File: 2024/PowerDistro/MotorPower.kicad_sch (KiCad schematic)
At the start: 8 parts, among them J1 10159560-A00221RLF, J2 10159560-A00221RLF, J3 10159560-A00221RLF, J4 10159560-A00221RLF, J5 10159560-A00221RLF, J6 10159560-A00221RLF, J7 10159560-A00221RLF, J8 10159560-A00221RLF

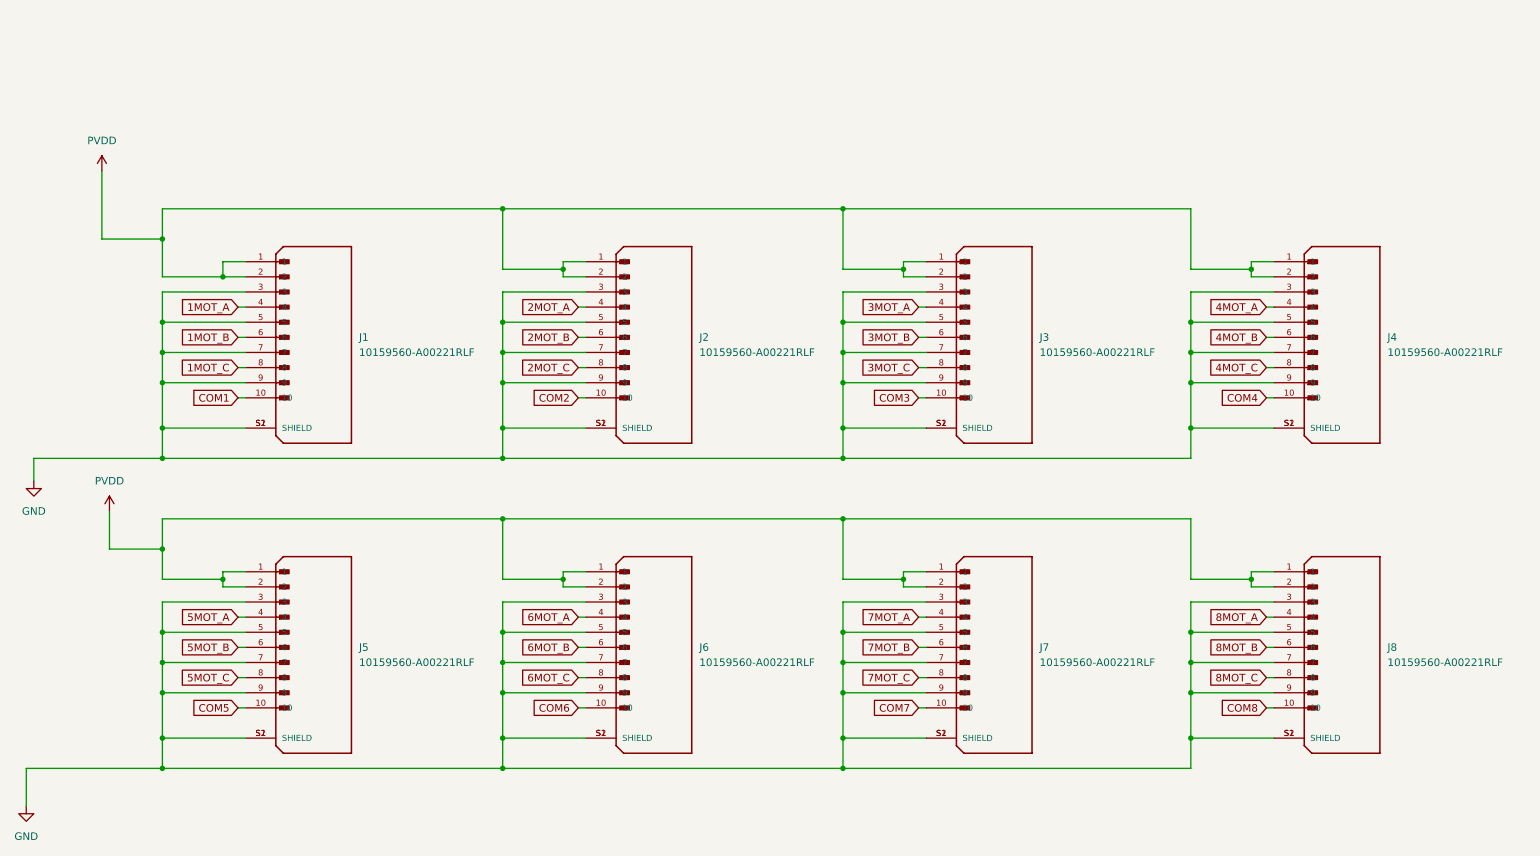
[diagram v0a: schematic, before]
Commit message: Added PCA pinout schematics
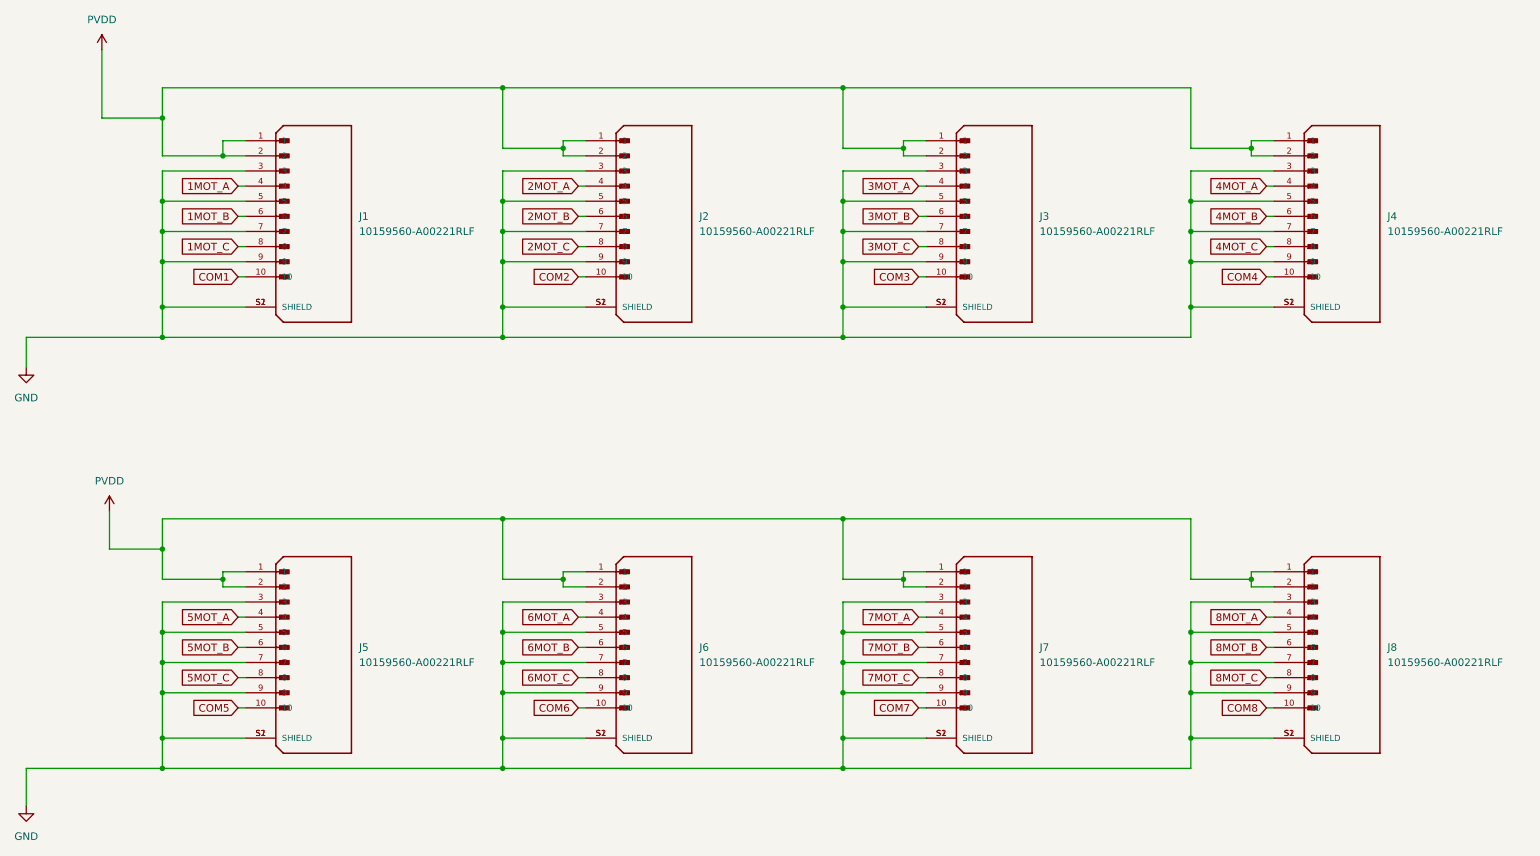
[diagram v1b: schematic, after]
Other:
- moved on the sheet: J1, J2, J3, J4

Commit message: Added EASYBldc Outlines
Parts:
- J1, J2, J3, J4, J5, J6, J7, J8: footprint 10159560-A00221RLF:AMPHENOL_10159560-A00221RLF -> PowerDistroFootprints:AMPHENOL_10159560-A00221RLF
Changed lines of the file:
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@@
 			)
 		)
-		(property "Footprint" "10159560-A00221RLF:AMPHENOL_10159560-A00221RLF"
+		(property "Footprint" "PowerDistroFootprints:AMPHENOL_10159560-A00221RLF"
 			(at 181.61 137.16 0)
 			(effects
@@
 			)
 		)
-		(property "Footprint" "10159560-A00221RLF:AMPHENOL_10159560-A00221RLF"
+		(property "Footprint" "PowerDistroFootprints:AMPHENOL_10159560-A00221RLF"
 			(at 124.46 64.77 0)
 			(effects
@@
 			)
 		)
-		(property "Footprint" "10159560-A00221RLF:AMPHENOL_10159560-A00221RLF"
+		(property "Footprint" "PowerDistroFootprints:AMPHENOL_10159560-A00221RLF"
 			(at 181.61 64.77 0)
 			(effects
@@
 			)
 		)
-		(property "Footprint" "10159560-A00221RLF:AMPHENOL_10159560-A00221RLF"
+		(property "Footprint" "PowerDistroFootprints:AMPHENOL_10159560-A00221RLF"
 			(at 240.03 64.77 0)
 			(effects
@@
 			)
 		)
-		(property "Footprint" "10159560-A00221RLF:AMPHENOL_10159560-A00221RLF"
+		(property "Footprint" "PowerDistroFootprints:AMPHENOL_10159560-A00221RLF"
 			(at 240.03 137.16 0)
 			(effects
@@
 			)
 		)
-		(property "Footprint" "10159560-A00221RLF:AMPHENOL_10159560-A00221RLF"
+		(property "Footprint" "PowerDistroFootprints:AMPHENOL_10159560-A00221RLF"
 			(at 67.31 137.16 0)
 			(effects
@@
 			)
 		)
-		(property "Footprint" "10159560-A00221RLF:AMPHENOL_10159560-A00221RLF"
+		(property "Footprint" "PowerDistroFootprints:AMPHENOL_10159560-A00221RLF"
 			(at 124.46 137.16 0)
 			(effects
@@
 			)
 		)
-		(property "Footprint" "10159560-A00221RLF:AMPHENOL_10159560-A00221RLF"
+		(property "Footprint" "PowerDistroFootprints:AMPHENOL_10159560-A00221RLF"
 			(at 67.31 64.77 0)
 			(effects

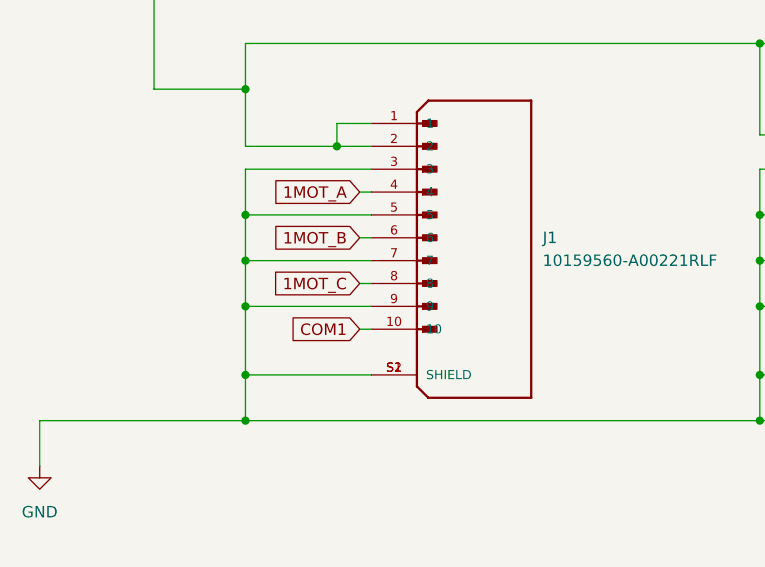
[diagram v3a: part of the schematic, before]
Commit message: Added connectors and esc footprints
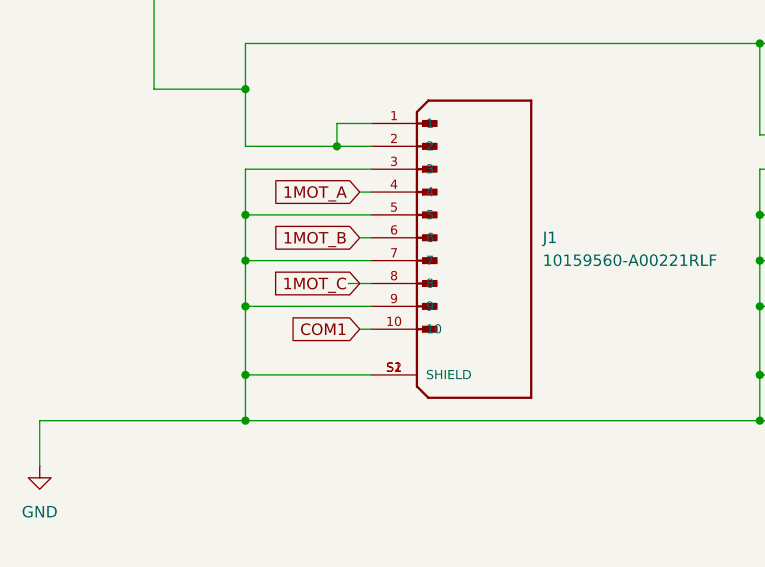
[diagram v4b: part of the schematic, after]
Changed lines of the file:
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@@
 	(wire
 		(pts
-			(xy 60.96 69.85) (xy 62.23 69.85)
+			(xy 59.69 69.85) (xy 62.23 69.85)
 		)
 		(stroke

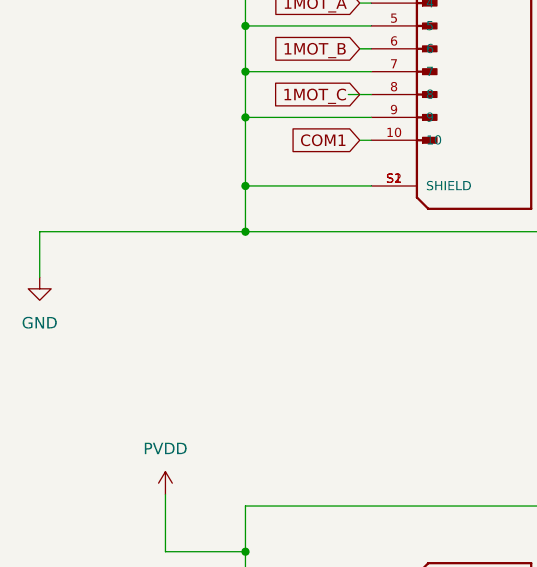
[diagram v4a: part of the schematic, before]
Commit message: Added power layer to power distro motors
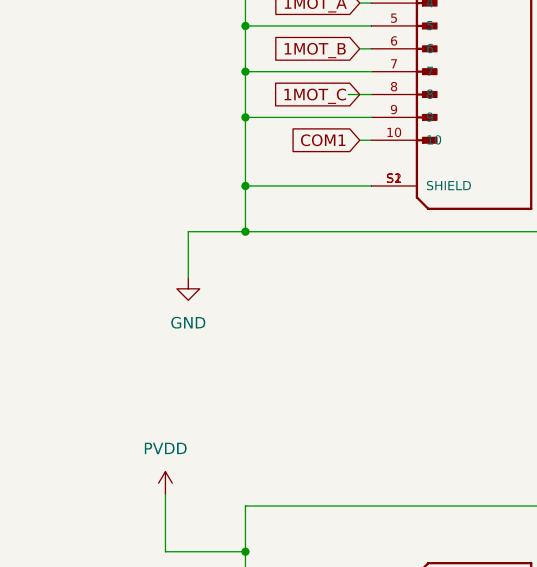
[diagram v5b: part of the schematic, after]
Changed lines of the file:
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@@
 	(wire
 		(pts
-			(xy 25.4 85.09) (xy 48.26 85.09)
+			(xy 41.91 85.09) (xy 48.26 85.09)
 		)
 		(stroke
@@
 	(wire
 		(pts
-			(xy 25.4 85.09) (xy 25.4 90.17)
+			(xy 41.91 85.09) (xy 41.91 90.17)
 		)
 		(stroke
@@
 	(symbol
 		(lib_id "power:GND")
-		(at 25.4 90.17 0)
+		(at 41.91 90.17 0)
 		(unit 1)
 		(exclude_from_sim no)
@@
 		(fields_autoplaced yes)
 		(property "Reference" "#PWR03"
-			(at 25.4 96.52 0)
+			(at 41.91 96.52 0)
 			(effects
 				(font
@@
 		)
 		(property "Value" "GND"
-			(at 25.4 95.25 0)
+			(at 41.91 95.25 0)
 			(effects
 				(font
@@
 		)
 		(property "Footprint" ""
-			(at 25.4 90.17 0)
+			(at 41.91 90.17 0)
 			(effects
 				(font
@@
 		)
 		(property "Datasheet" ""
-			(at 25.4 90.17 0)
+			(at 41.91 90.17 0)
 			(effects
 				(font
@@
 		)
 		(property "Description" "Power symbol creates a global label with name \"GND\" , ground"
-			(at 25.4 90.17 0)
-			(effects
-				(font
+			(at 41.91 90.17 0)
+			(effects
+				(font

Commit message: Changed Everything
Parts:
- removed J1, J2, J3, J4, J5, J6, J7, J8: 10159560-A00221RLF, PowerDistroFootprints:AMPHENOL_10159560-A00221RLF, symbol PowerDistro:10159560-A00221RLF
